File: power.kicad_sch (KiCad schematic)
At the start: 6 parts, among them U3 TPS62056DGS

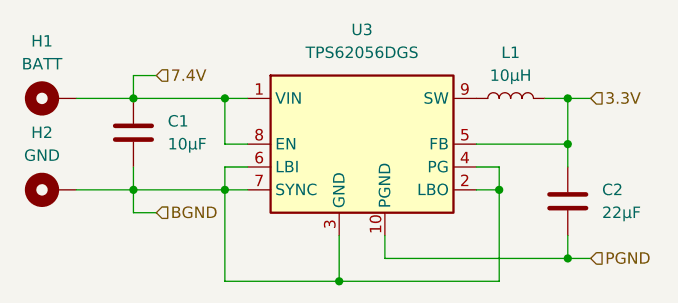
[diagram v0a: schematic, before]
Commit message: Update references and switch to higher power MOSFETS
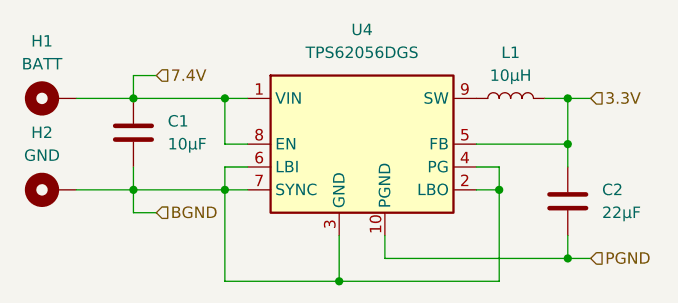
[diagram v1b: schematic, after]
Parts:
- renumbered U3 to U4
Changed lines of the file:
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@@
 		(dnp no)
 		(fields_autoplaced yes)
-		(property "Reference" "U3"
+		(property "Reference" "U4"
 			(at 147.32 78.74 0)
 			(effects
@@
 			(project "rocket"
 				(path "/d94d1fd0-ec09-478b-a1a4-3306111fc872/fe9aeed3-ff94-4ab2-b0b9-a506c2c9279b"
-					(reference "U3")
+					(reference "U4")
 					(unit 1)
 				)

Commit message: Begin PCB work
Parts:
- H1: footprint MountingHole:MountingHole_2.2mm_M2_ISO7380_Pad_TopBottom -> MountingHole:MountingHole_2.5mm_Pad
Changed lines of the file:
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@@
 			)
 		)
-		(property "Footprint" "MountingHole:MountingHole_2.2mm_M2_ISO7380_Pad_TopBottom"
+		(property "Footprint" "MountingHole:MountingHole_2.5mm_Pad"
 			(at 113.03 86.36 0)
 			(effects
